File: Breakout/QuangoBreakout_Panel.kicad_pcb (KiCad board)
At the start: 2 copper layers, 20.3 x 128.5 mm, 23 parts

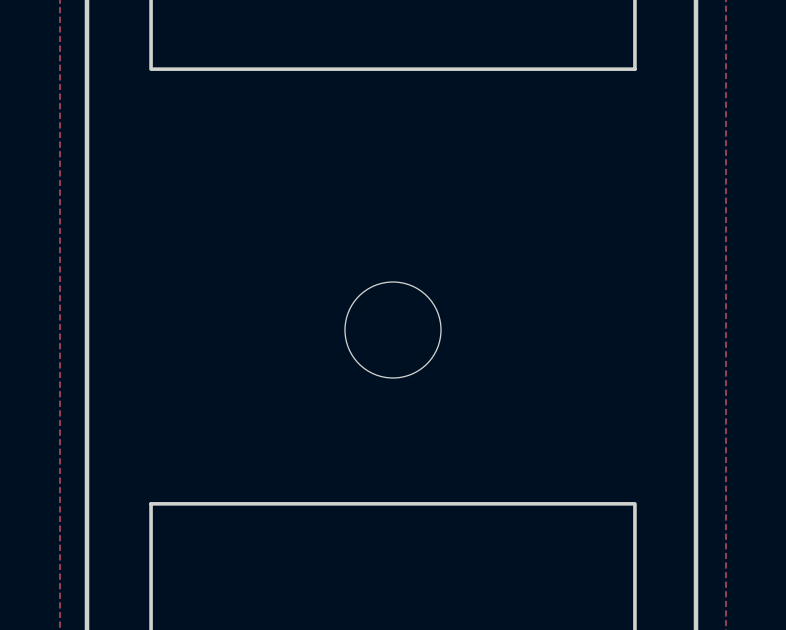
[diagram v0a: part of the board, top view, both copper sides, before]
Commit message: Terminated unused op-amp
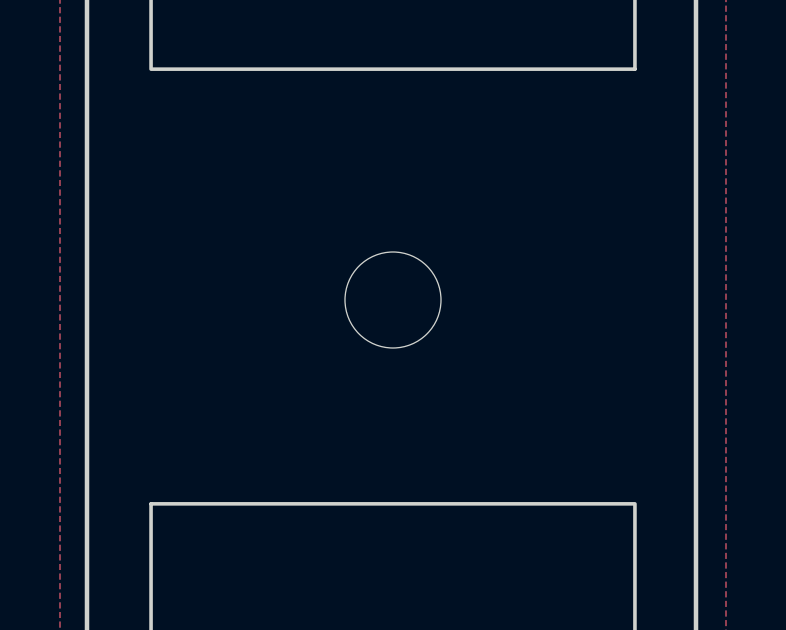
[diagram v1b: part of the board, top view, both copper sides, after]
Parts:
- removed kibuzzard-6498108F: G***, kibuzzard-6498108F
- removed kibuzzard-649810A1: G***, kibuzzard-649810A1
- removed kibuzzard-649810AB: G***, kibuzzard-649810AB
- removed kibuzzard-64981165 (x2): G***, kibuzzard-64981165
- removed kibuzzard-6498118B (x2): G***, kibuzzard-6498118B
- removed kibuzzard-64985DE2: G***, kibuzzard-64985DE2
- removed kibuzzard-64985E01: G***, kibuzzard-64985E01
- added kibuzzard-649866B8: G***, kibuzzard-649866B8, F.Cu at (59.4, 162.1)
- added kibuzzard-649866DB: G***, kibuzzard-649866DB, F.Cu at (54.7, 134.5)
- added kibuzzard-649866EF: G***, kibuzzard-649866EF, F.Cu at (64.1, 134.5)
- added kibuzzard-649869A1: G***, kibuzzard-649869A1, F.Cu at (52.8, 87.9)
- added kibuzzard-649869D7: G***, kibuzzard-649869D7, F.Cu at (65.9, 91.4)
- moved H1 1.00 mm to (59.4, 90.9)
- moved kibuzzard-64985CD8 0.10 mm to (53.5, 112.7)
- moved kibuzzard-64985CE4 0.10 mm to (65.5, 114.0)
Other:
- board text added: "Mountjoy Modular"
- board text added: "Quango Breakout"
- board text added: "Quango Breakout Panel 2023"
- board text removed: "Breakout"
- board text removed: "Mountjoy"

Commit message: Panel labelling
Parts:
- removed kibuzzard-649866B8: G***, kibuzzard-649866B8
- removed kibuzzard-649866DB: G***, kibuzzard-649866DB
- removed kibuzzard-649866EF: G***, kibuzzard-649866EF
- added G***: LOGO, Graphics:QuangoLogoSmall, F.Cu at (59.6, 133.5)
- added kibuzzard-649954C4: G***, kibuzzard-649954C4, F.Cu at (59.4, 162.1)
- added kibuzzard-64995539: G***, kibuzzard-64995539, F.Cu at (54.7, 148.3)
- added kibuzzard-6499554E: G***, kibuzzard-6499554E, F.Cu at (64.1, 148.3)
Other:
- board text removed: "Quango Breakout"
- board text removed: "SEND"
